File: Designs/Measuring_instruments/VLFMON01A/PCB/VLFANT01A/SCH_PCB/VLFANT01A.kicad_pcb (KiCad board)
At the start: 2 copper layers, 30 x 40.1 mm, 13 parts, among them J1 CONN_3, J2 CONN_3, J3 CONN_3, J4 CONN_3, J5 CONN_3, J6 CONN_3, J7 SMA, J8 CONN_3, J9 JUMP_3X2, M1 HOLE, M2 HOLE, M3 HOLE, M4 HOLE

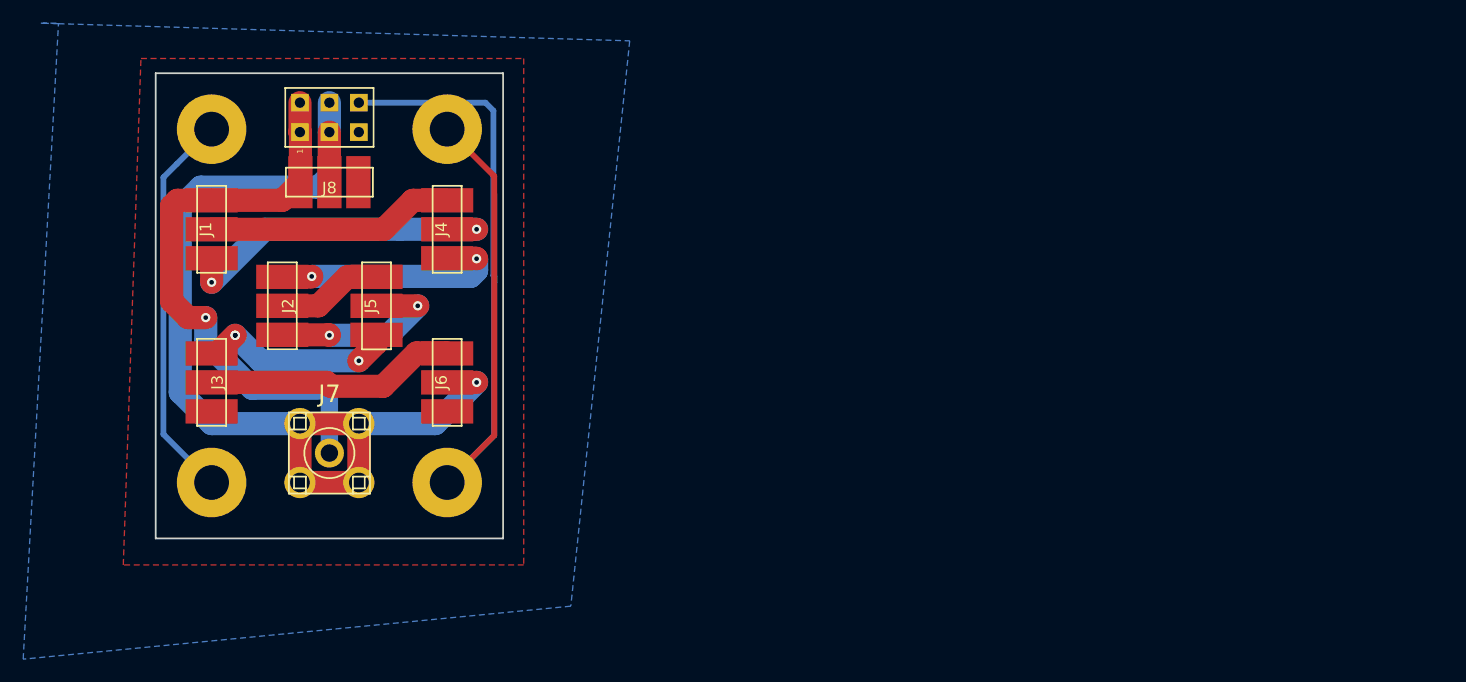
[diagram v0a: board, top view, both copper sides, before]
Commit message: 
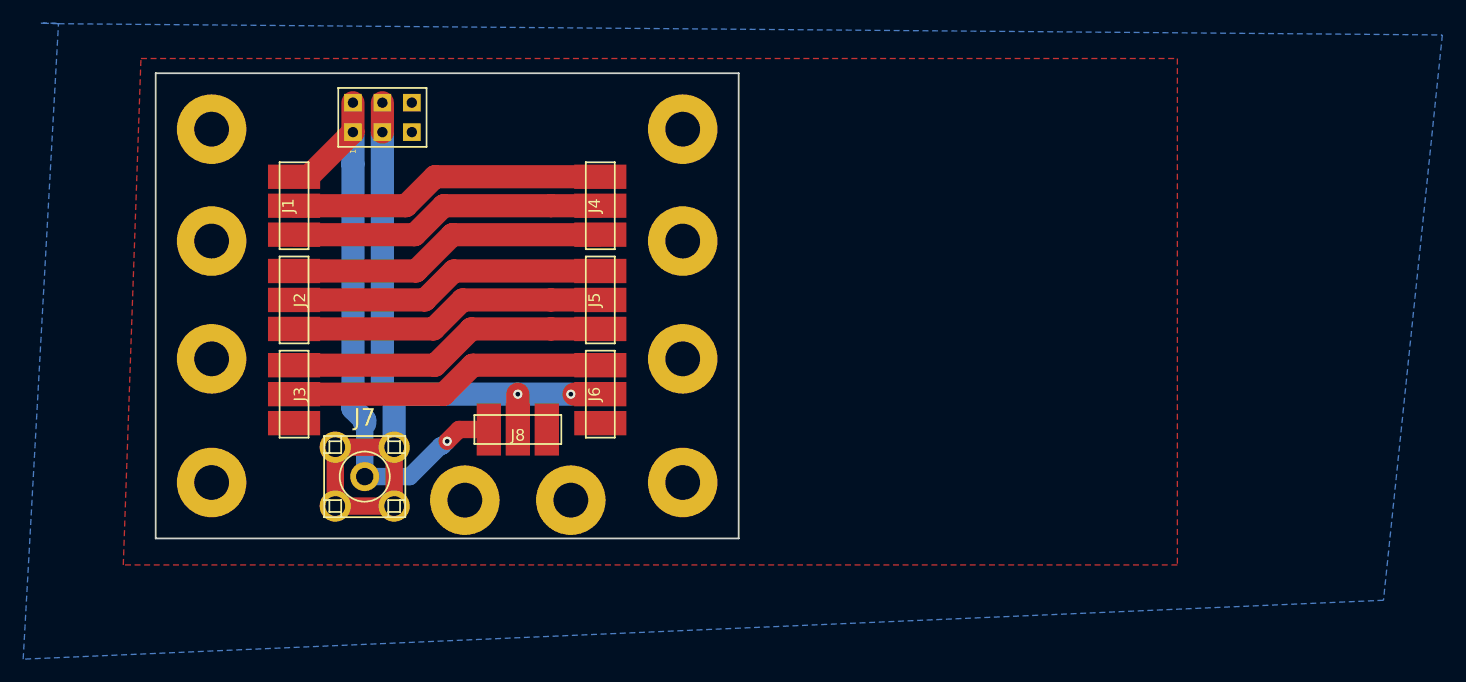
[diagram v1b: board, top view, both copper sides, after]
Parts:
- added M10: HOLE, Mlab_Mechanical:MountingHole_3mm, F.Cu at (26.9, -3.56)
- added M5: HOLE, Mlab_Mechanical:MountingHole_3mm, F.Cu at (45.7, -25.9)
- added M6: HOLE, Mlab_Mechanical:MountingHole_3mm, F.Cu at (45.7, -15.7)
- added M7: HOLE, Mlab_Mechanical:MountingHole_3mm, F.Cu at (5.08, -25.9)
- added M8: HOLE, Mlab_Mechanical:MountingHole_3mm, F.Cu at (5.08, -15.7)
- added M9: HOLE, Mlab_Mechanical:MountingHole_3mm, F.Cu at (36.1, -3.56)
- moved J8 26.8 mm to (31.5, -9.65)
- moved M1 20.3 mm to (45.7, -35.6)
- moved M2 20.3 mm to (45.7, -5.08)
- moved J5 19.3 mm to (38.6, -20.8)
- moved J4 13.4 mm to (38.6, -29.0)
- moved J6 13.2 mm to (38.6, -12.7)
- moved J1 7.40 mm to (12.2, -29.0)
- moved J3 7.18 mm to (12.2, -12.7)
- moved J9 4.57 mm to (19.8, -36.6)
- moved J7 3.66 mm to (18.3, -5.59)
- moved J2 1.14 mm to (12.2, -20.8)
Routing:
- net GND: track 121.1 -> 0.00 mm
- net /4: track 9.16 -> 27.5 mm
- net /OUT2: track 86.5 -> 72.2 mm, vias 1 -> 2
- net /5: track 16.3 -> 27.5 mm, vias 2 -> 0
- net /6: track 17.2 -> 27.7 mm, vias 3 -> 0
- net /3: track 20.6 -> 27.7 mm, vias 2 -> 0
- net /1: track 21.4 -> 27.5 mm
- net /7: track 21.7 -> 27.5 mm
- net /2: track 29.4 -> 27.5 mm, vias 2 -> 0
- net /OUT1: track 50.3 -> 51.7 mm
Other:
- board size 30 x 40.1 mm -> 50.3 x 40.1 mm
- net class Default: clearance 0.2 -> 0.3
- rule trace_clearance: 0.2 -> 0.3

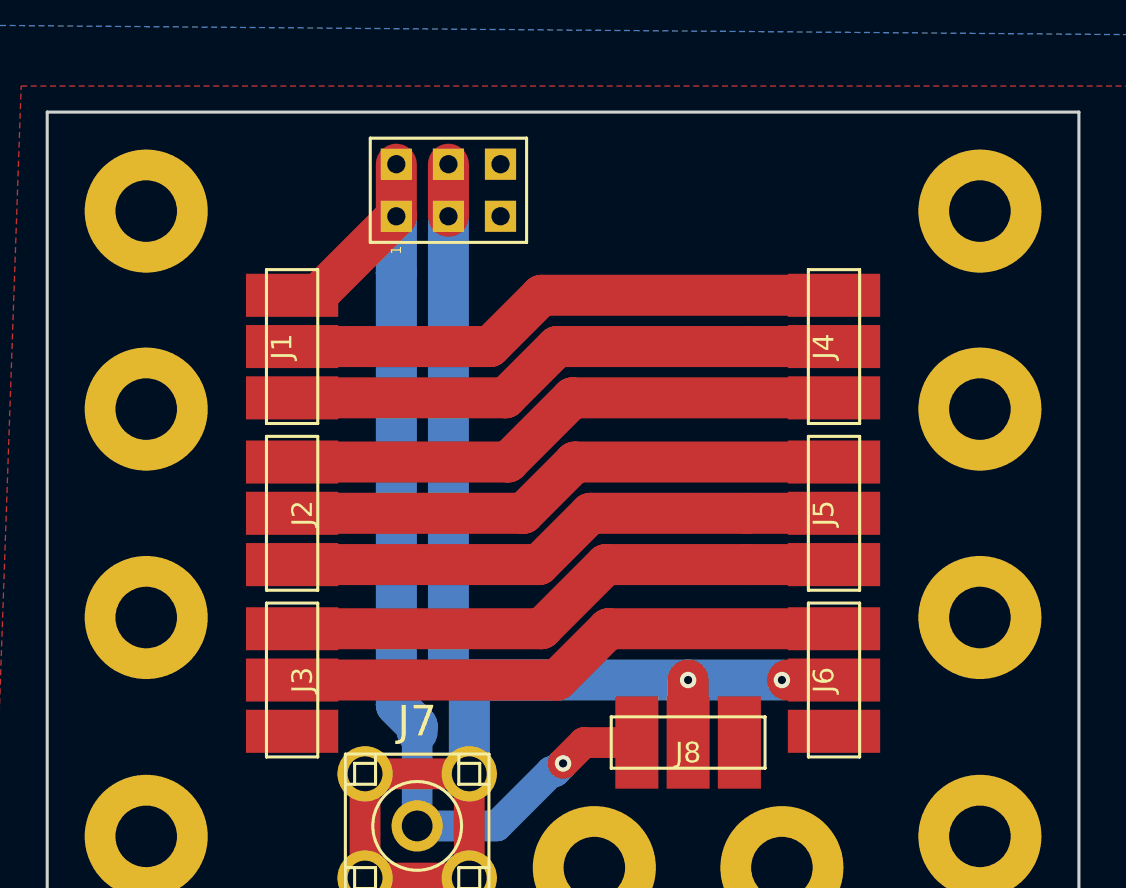
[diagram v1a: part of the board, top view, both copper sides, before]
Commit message: 
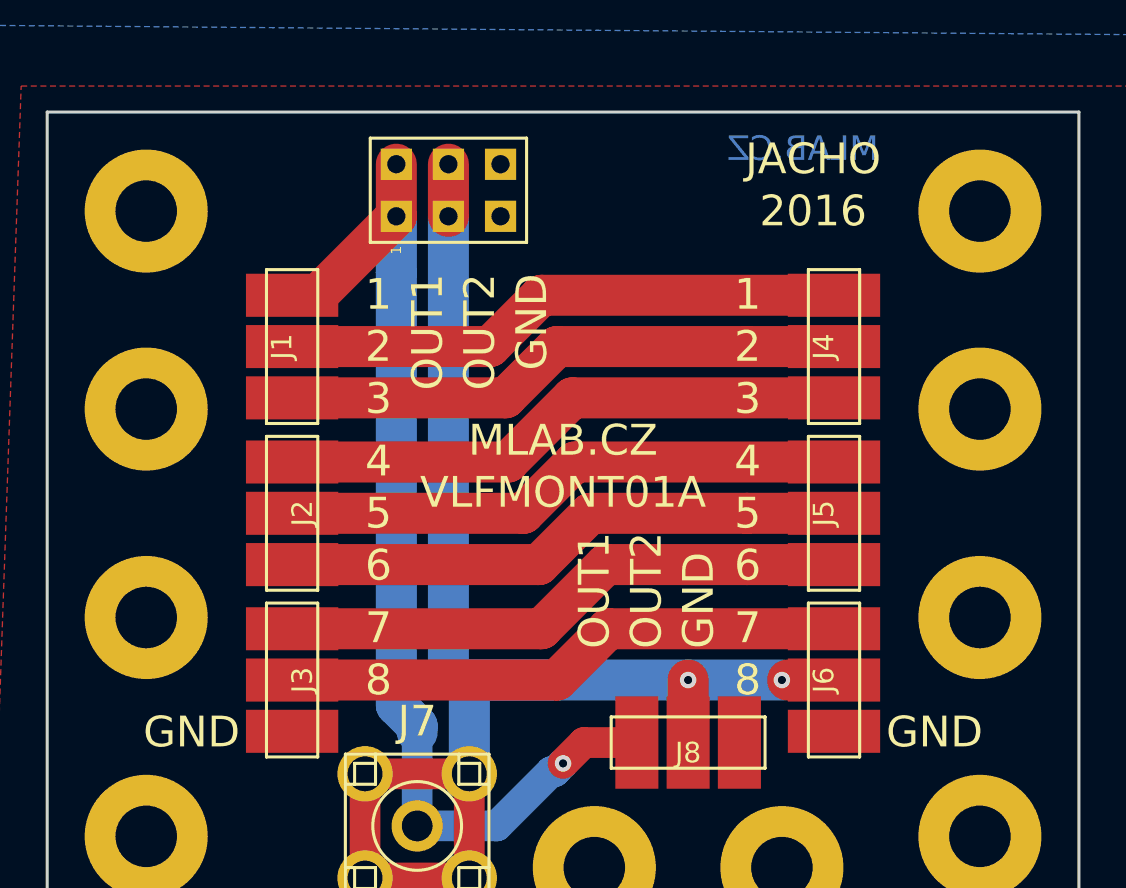
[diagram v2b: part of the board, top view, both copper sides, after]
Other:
- board text added: "1"
- board text added: "2"
- board text added: "2016"
- board text added: "3"
- board text added: "4"
- board text added: "5"
- board text added: "6"
- board text added: "7"
- board text added: "8"
- board text added: "GND"
- board text added: "JACHO"
- board text added: "MLAB.CZ"
- board text added: "OUT1"
- board text added: "OUT2"
- board text added: "VLFMONT01A"
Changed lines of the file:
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@@
     (links 32)
     (no_connects 0)
-    (area 0.178999 -40.461001 50.621001 -0.178999)
+    (area -11.176 -44.704 111.252001 10.160001)
     (thickness 1.6)
-    (drawings 4)
+    (drawings 33)
     (tracks 54)
     (zones 0)
@@
   )
   (setup
-    (last_trace_width 1.5)
+    (last_trace_width 0.25)
     (user_trace_width 0.5)
     (user_trace_width 0.8)
@@
     (pad_drill 3)
     (pad_to_mask_clearance 0.2)
+    (solder_mask_min_width 0.2)
     (aux_axis_origin 0 0)
     (visible_elements 7FFFFF7F)
     (pcbplotparams
-      (layerselection 0x00030_80000001)
+      (layerselection 0x010e0_80000001)
       (usegerberextensions false)
       (excludeedgelayer true)
@@
       (outputformat 1)
       (mirror false)
-      (drillshape 1)
+      (drillshape 0)
       (scaleselection 1)
-      (outputdirectory ""))
+      (outputdirectory ../CAM_PROFI/))
   )
   (net 0 "")
@@
       (net 7 GND) (clearance 1) (zone_connect 2))
   )
+  (gr_text MLAB.CZ (at 37.084 -38.608) (layer B.Cu)
+    (effects (font (size 1.2 1.2) (thickness 0.3)) (justify mirror))
+  )
+  (gr_text 2016 (at 37.592 -35.56) (layer F.SilkS)
+    (effects (font (size 1.5 1.5) (thickness 0.3)))
+  )
+  (gr_text JACHO (at 37.592 -38.1) (layer F.SilkS)
+    (effects (font (size 1.5 1.5) (thickness 0.3)))
+  )
+  (gr_text VLFMONT01A (at 25.4 -21.844) (layer F.SilkS)
+    (effects (font (size 1.5 1.5) (thickness 0.3)))
+  )
+  (gr_text MLAB.CZ (at 25.4 -24.384) (layer F.SilkS)
+    (effects (font (size 1.5 1.5) (thickness 0.3)))
+  )
+  (gr_text GND (at 23.876 -32.512 90) (layer F.SilkS)
+    (effects (font (size 1.5 1.5) (thickness 0.3)) (justify right))
+  )
+  (gr_text OUT2 (at 21.336 -32.512 90) (layer F.SilkS)
+    (effects (font (size 1.5 1.5) (thickness 0.3)) (justify right))
+  )
+  (gr_text OUT1 (at 18.796 -32.512 90) (layer F.SilkS)
+    (effects (font (size 1.5 1.5) (thickness 0.3)) (justify right))
+  )
+  (gr_text GND (at 32.004 -14.224 90) (layer F.SilkS)
+    (effects (font (size 1.5 1.5) (thickness 0.3)) (justify left))
+  )
+  (gr_text OUT2 (at 29.464 -14.224 90) (layer F.SilkS)
+    (effects (font (size 1.5 1.5) (thickness 0.3)) (justify left))
+  )
+  (gr_text OUT1 (at 26.924 -14.224 90) (layer F.SilkS)
+    (effects (font (size 1.5 1.5) (thickness 0.3)) (justify left))
+  )
+  (gr_text GND (at 41.148 -10.16) (layer F.SilkS)
+    (effects (font (size 1.5 1.5) (thickness 0.3)) (justify left))
+  )
+  (gr_text GND (at 9.652 -10.16) (layer F.SilkS)
+    (effects (font (size 1.5 1.5) (thickness 0.3)) (justify right))
+  )
+  (gr_text 8 (at 35.052 -12.7) (layer F.SilkS)
+    (effects (font (size 1.5 1.5) (thickness 0.3)) (justify right))
+  )
+  (gr_text 7 (at 35.052 -15.24) (layer F.SilkS)
+    (effects (font (size 1.5 1.5) (thickness 0.3)) (justify right))
+  )
+  (gr_text 6 (at 35.052 -18.288) (layer F.SilkS)
+    (effects (font (size 1.5 1.5) (thickness 0.3)) (justify right))
+  )
+  (gr_text 5 (at 35.052 -20.828) (layer F.SilkS)
+    (effects (font (size 1.5 1.5) (thickness 0.3)) (justify right))
+  )
+  (gr_text 4 (at 35.052 -23.368) (layer F.SilkS)
+    (effects (font (size 1.5 1.5) (thickness 0.3)) (justify right))
+  )
+  (gr_text 3 (at 35.052 -26.416) (layer F.SilkS)
+    (effects (font (size 1.5 1.5) (thickness 0.3)) (justify right))
+  )
+  (gr_text 2 (at 35.052 -28.956) (layer F.SilkS)
+    (effects (font (size 1.5 1.5) (thickness 0.3)) (justify right))
+  )
+  (gr_text 1 (at 35.052 -31.496) (layer F.SilkS)
+    (effects (font (size 1.5 1.5) (thickness 0.3)) (justify right))
+  )
+  (gr_text 8 (at 15.748 -12.7) (layer F.SilkS)
+    (effects (font (size 1.5 1.5) (thickness 0.3)) (justify left))
+  )
+  (gr_text 7 (at 15.748 -15.24) (layer F.SilkS)
+    (effects (font (size 1.5 1.5) (thickness 0.3)) (justify left))
+  )
+  (gr_text 6 (at 15.748 -18.288) (layer F.SilkS)
+    (effects (font (size 1.5 1.5) (thickness 0.3)) (justify left))
+  )
+  (gr_text 5 (at 15.748 -20.828) (layer F.SilkS)
+    (effects (font (size 1.5 1.5) (thickness 0.3)) (justify left))
+  )
+  (gr_text 4 (at 15.748 -23.368) (layer F.SilkS)
+    (effects (font (size 1.5 1.5) (thickness 0.3)) (justify left))
+  )
+  (gr_text 3 (at 15.748 -26.416) (layer F.SilkS)
+    (effects (font (size 1.5 1.5) (thickness 0.3)) (justify left))
+  )
+  (gr_text 2 (at 15.748 -28.956) (layer F.SilkS)
+    (effects (font (size 1.5 1.5) (thickness 0.3)) (justify left))
+  )
+  (gr_text 1 (at 15.748 -31.496) (layer F.SilkS)
+    (effects (font (size 1.5 1.5) (thickness 0.3)) (justify left))
+  )
   (gr_line (start 0.254 -0.254) (end 0.254 -40.386) (angle 90) (layer Edge.Cuts) (width 0.15))
